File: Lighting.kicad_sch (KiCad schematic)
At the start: 14 parts, among them Q2 2N7002, Q5 2N7002, U2 SI8261ABC-IS, U4 SI8261ABC-IS

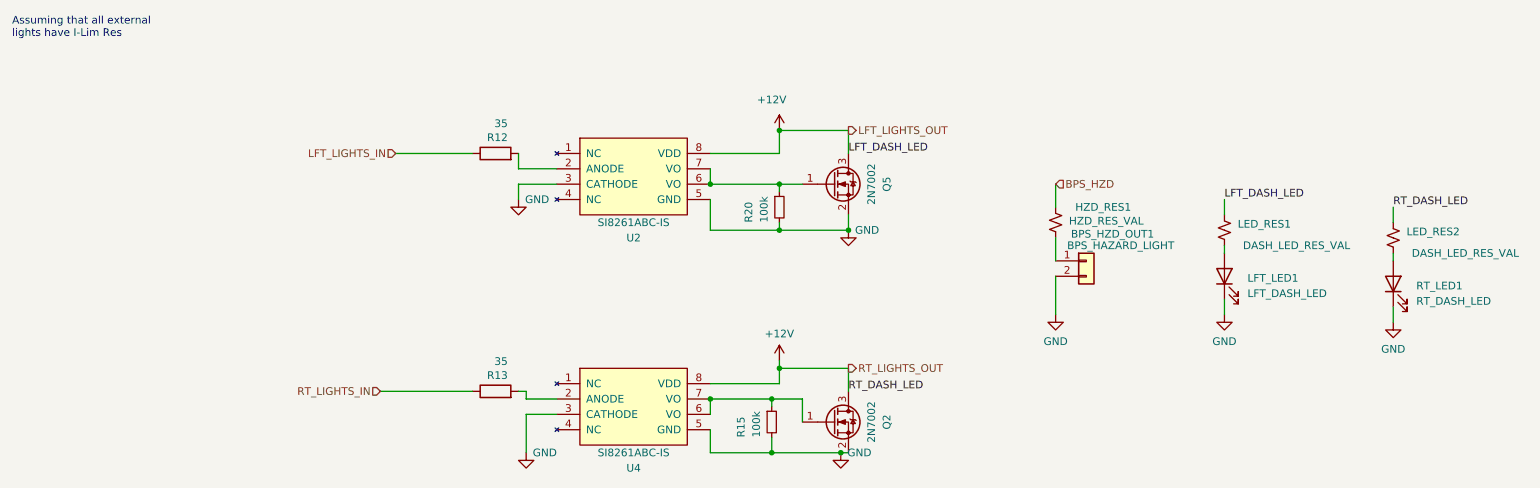
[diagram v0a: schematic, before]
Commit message: Update 1/2
Fixed some of the requested changes.
Still need to fix it up a bit more.
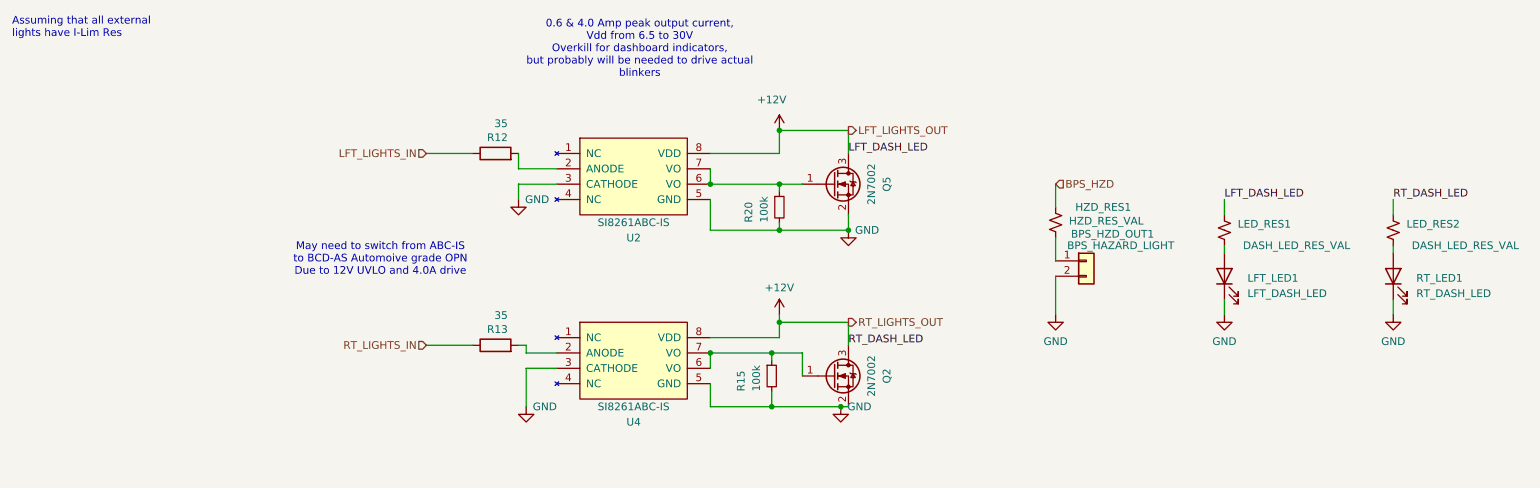
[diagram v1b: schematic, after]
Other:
- note added: "0.6 & 4.0 Amp peak output current, Vdd from 6.5 to 30V Overkill for dashboard indicators, but probably will be needed to drive actual blinkers"
- note added: "May need to switch from ABC-IS to BCD-AS Automoive grade OPN Due to 12V UVLO and 4.0A drive"
- moved on the sheet: LED_RES2, Q2, R13, R15, RT_LED1, U4

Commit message: Ready for review
Controls decided to move a bunch of stuff back to leaderboard, also I think I fixed everything else.
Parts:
- removed BPS_HZD_OUT1: BPS_HAZARD_LIGHT, Connector_Molex:Molex_Micro-Fit_3.0_43650-0215_1x02_P3.00mm_Vertical, symbol Connector_Generic:Conn_01x02
- removed HZD_RES1: HZD_RES_VAL, Resistor_SMD:R_0805_2012Metric, symbol Device:R_Small_US
- removed LED_RES1, LED_RES2: DASH_LED_RES_VAL, Resistor_SMD:R_0805_2012Metric, symbol Device:R_Small_US
- removed LFT_LED1: LFT_DASH_LED, symbol Device:LED
- removed Q2, Q5: 2N7002, Package_TO_SOT_SMD:SOT-23, symbol Transistor_FET:2N7002
- removed R12, R13: 35, Resistor_SMD:R_0805_2012Metric, symbol Device:R
- removed R15, R20: 100k, Resistor_SMD:R_0805_2012Metric, symbol Device:R_Small
- removed RT_LED1: RT_DASH_LED, symbol Device:LED
- removed U2, U4: SI8261ABC-IS, Package_SO:SOIC-8_3.9x4.9mm_P1.27mm, symbol utsvt-bps:SI8261ABC-IS
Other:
- note removed: "0.6 & 4.0 Amp peak output current, Vdd from 6.5 to 30V Overkill for dashboard indicators, but probably will be needed to drive actual blinkers"
- note removed: "Assuming that all external lights have I-Lim Res"
- note removed: "May need to switch from ABC-IS to BCD-AS Automoive grade OPN Due to 12V UVLO and 4.0A drive"
